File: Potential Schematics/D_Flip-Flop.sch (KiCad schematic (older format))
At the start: 1 part, among them U18 74LS04

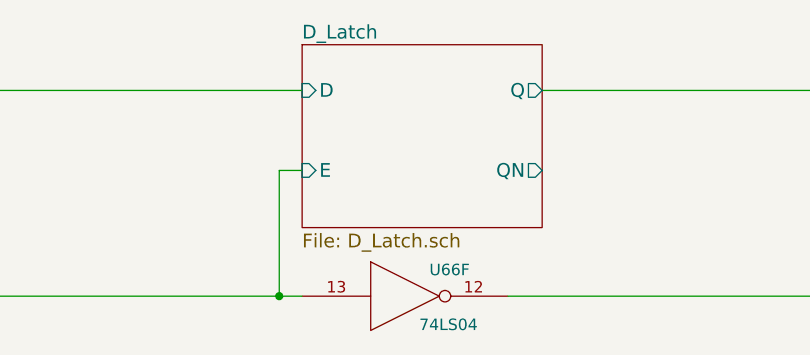
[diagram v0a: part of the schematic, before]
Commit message: Added Registers to Top Schematic
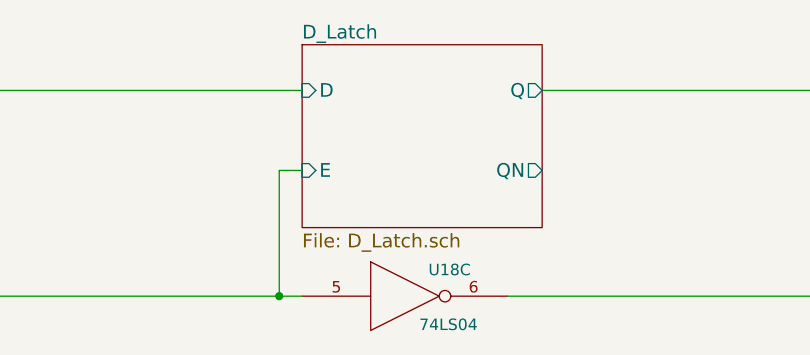
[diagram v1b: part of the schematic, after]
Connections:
- net C: now also U18.5; no longer U18.13
- net D_Latch/E: now also U18.6; no longer U18.12
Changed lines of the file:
@@
 $Descr A4 11693 8268
 encoding utf-8
-Sheet 130 449
+Sheet 25 449
 Title "D Flip-Flop"
 Date "2018-09-14"
@@
 $Comp
 L 74LS04 U18
-U 6 1 5B9C36D9
+U 3 1 5B9C36D9
 P 4450 4300
 AR Path="/5B9D167A/5B9C0EA0/5B9C0F16/5B9C0F19/5B9C36D9" Ref="U18"  Part="3"
@@
 AR Path="/5B9D167A/5B9C0EA0/5B9DB28B/5B9C41D5/5B9C36D9" Ref="U171"  Part="6"
 AR Path="/5B9D167A/5B9C0EA0/5B9DB28B/5B9C41DB/5B9C36D9" Ref="U176"  Part="3"
-F 0 "U66" H 4645 4415 50  0000 C CNN
+F 0 "U18" H 4645 4415 50  0000 C CNN
 F 1 "74LS04" H 4640 4175 50  0000 C CNN
 F 2 "" H 4450 4300 50  0001 C CNN
 F 3 "" H 4450 4300 50  0001 C CNN
-	6    4450 4300
+	3    4450 4300
 	1    0    0    -1
 $EndComp

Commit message: Adding Multiply Devide
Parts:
- U18: symbol 74LS04 -> 4-bit_processor-rescue:74LS04
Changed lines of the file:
@@
-EESchema Schematic File Version 2
-LIBS:power
-LIBS:device
-LIBS:switches
-LIBS:relays
-LIBS:motors
-LIBS:transistors
-LIBS:conn
-LIBS:linear
-LIBS:regul
-LIBS:74xx
-LIBS:cmos4000
-LIBS:adc-dac
-LIBS:memory
-LIBS:xilinx
-LIBS:microcontrollers
-LIBS:dsp
-LIBS:microchip
-LIBS:analog_switches
-LIBS:motorola
-LIBS:texas
-LIBS:intel
-LIBS:audio
-LIBS:interface
-LIBS:digital-audio
-LIBS:philips
-LIBS:display
-LIBS:cypress
-LIBS:siliconi
-LIBS:opto
-LIBS:atmel
-LIBS:contrib
-LIBS:valves
+EESchema Schematic File Version 4
 LIBS:4-bit_processor-cache
-EELAYER 25 0
+EELAYER 26 0
 EELAYER END
 $Descr A4 11693 8268
 encoding utf-8
-Sheet 25 449
+Sheet 25 451
 Title "D Flip-Flop"
 Date "2018-09-14"
@@
 	1800 3400 4000 3400
 $Comp
-L 74LS04 U18
+L 4-bit_processor-rescue:74LS04 U18
 U 3 1 5B9C36D9
 P 4450 4300

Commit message: Finished PCB
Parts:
- U25: renamed from U18; footprint (none) -> Daniel_Kopp:DIP-14_300_ELL
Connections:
- net C: now also U25.13; no longer U25.5
- net D_Latch/E: now also U25.12; no longer U25.6

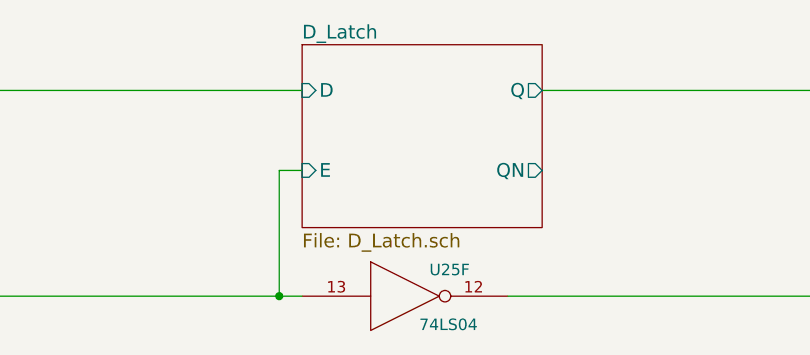
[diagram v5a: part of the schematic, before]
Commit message: Updated overview of Schematic
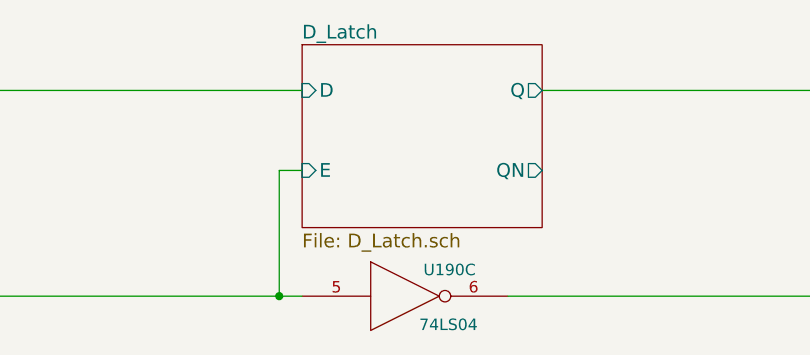
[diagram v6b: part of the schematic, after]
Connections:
- net C: now also U25.5; no longer U25.13
- net D_Latch/E: now also U25.6; no longer U25.12
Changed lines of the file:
@@
 $Descr A4 11693 8268
 encoding utf-8
-Sheet 25 467
+Sheet 25 902
 Title "D Flip-Flop"
 Date "2018-09-14"
@@
 $Comp
 L 4-bit_processor-rescue:74LS04 U25
-U 6 1 5B9C36D9
+U 3 1 5B9C36D9
 P 4450 4300
 AR Path="/5B9D167A/5B9C0EA0/5B9C0F16/5B9C0F19/5B9C36D9" Ref="U25"  Part="6"
@@
 AR Path="/5B9D167A/5B9C0EA0/5B9DB28B/5B9C41D5/5B9C36D9" Ref="U185"  Part="6"
 AR Path="/5B9D167A/5B9C0EA0/5B9DB28B/5B9C41DB/5B9C36D9" Ref="U190"  Part="3"
-F 0 "U25" H 4645 4415 50  0000 C CNN
+F 0 "U190" H 4645 4415 50  0000 C CNN
 F 1 "74LS04" H 4640 4175 50  0000 C CNN
 F 2 "Daniel_Kopp:DIP-14_300_ELL" H 4450 4300 50  0001 C CNN
 F 3 "" H 4450 4300 50  0001 C CNN
-	6    4450 4300
+	3    4450 4300
 	1    0    0    -1
 $EndComp
